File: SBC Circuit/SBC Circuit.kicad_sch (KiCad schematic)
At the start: 21 parts, among them J2 Conn_01x06_Pin, SW1 RESET, U1 MC68000FN, U11 MC34064P, X1 SG-531

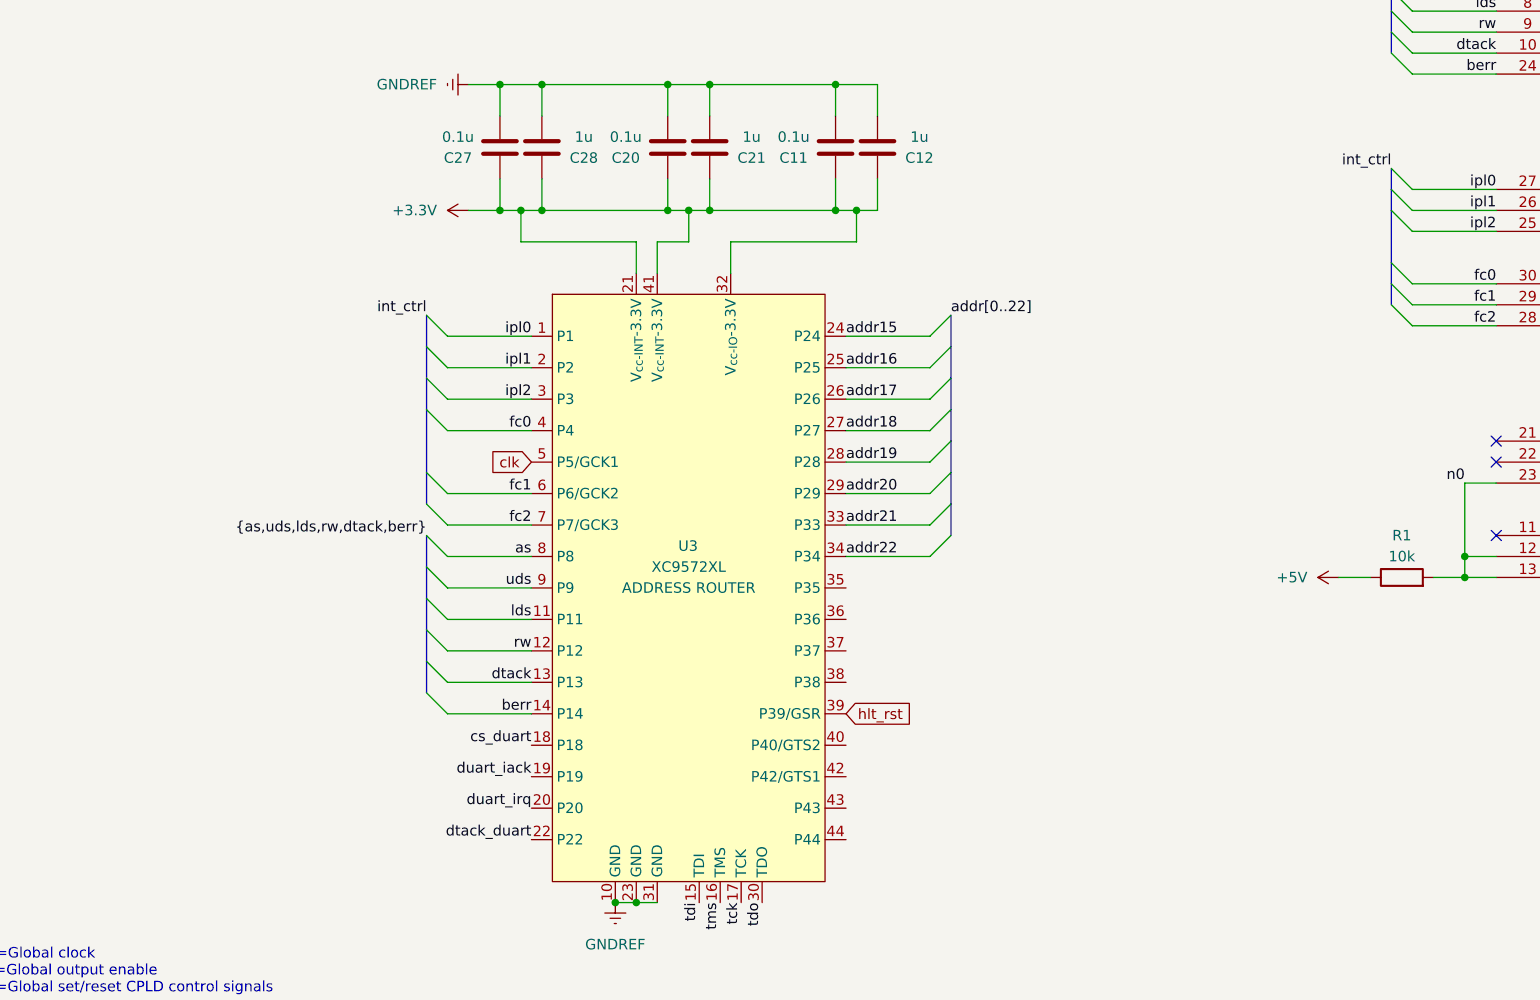
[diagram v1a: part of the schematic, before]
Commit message: New part selections, serial port selection
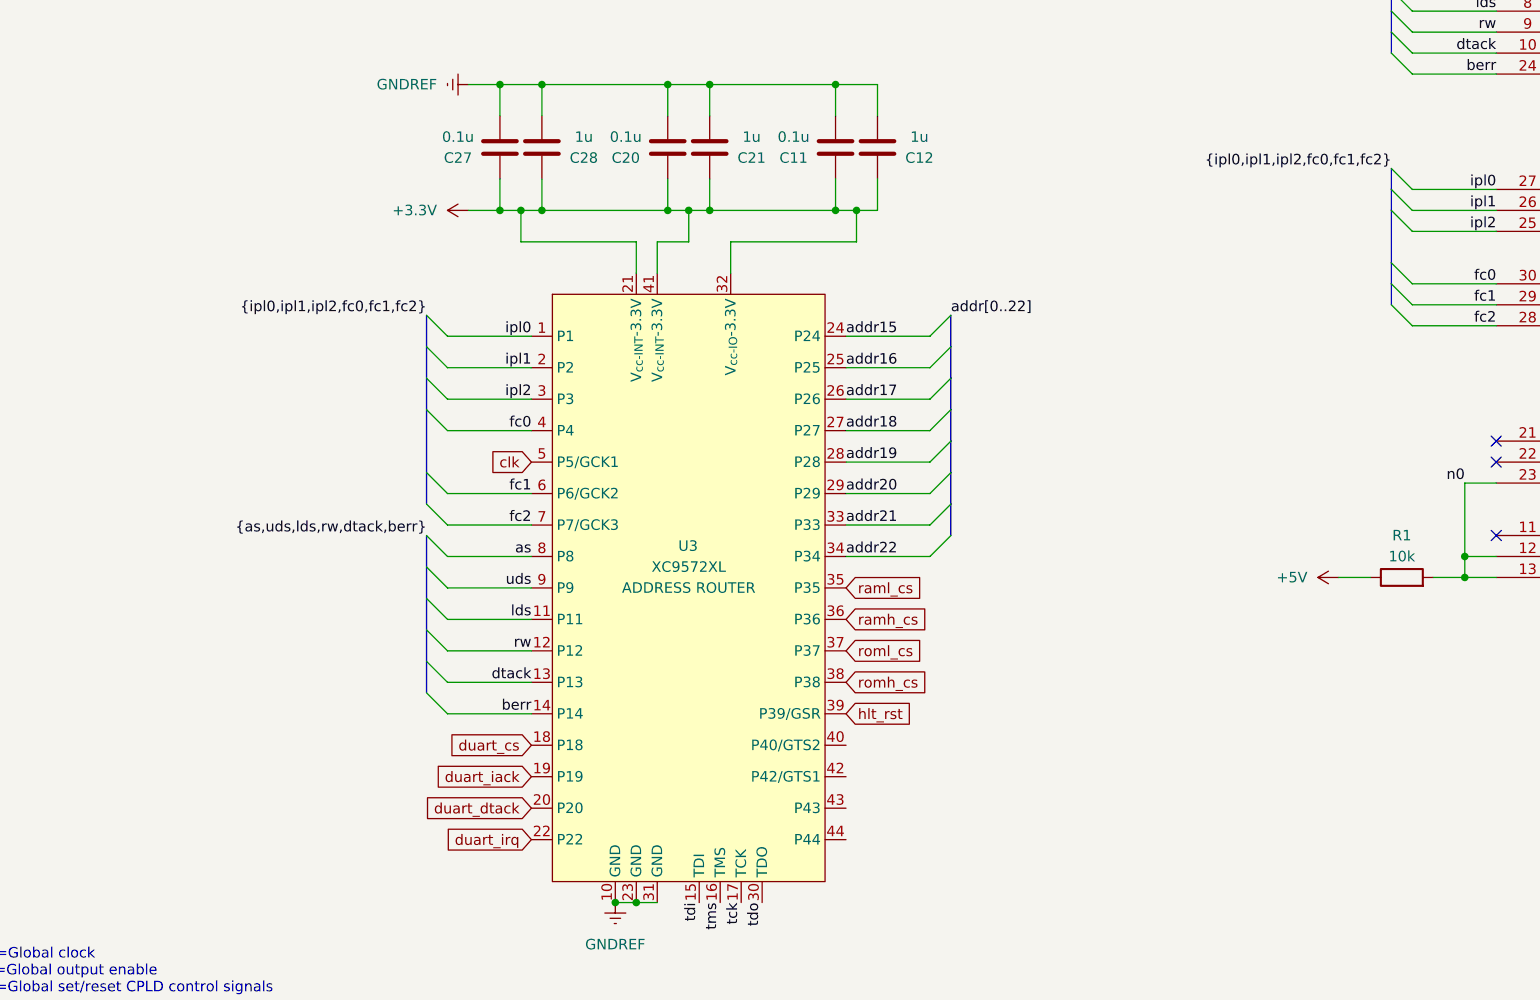
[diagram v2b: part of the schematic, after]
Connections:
- net dtack_duart is gone; now on net duart_irq: U3.22 (P22)
- net duart_irq: no longer U3.20 (P20)
- net raml_cs: now reaches U3.35 (P35)
- net ramh_cs: now reaches U3.36 (P36)
- net roml_cs: now reaches U3.37 (P37)
- net romh_cs: now reaches U3.38 (P38)
- net cs_duart renamed duart_cs
- new net duart_dtack: U3.20 (P20)

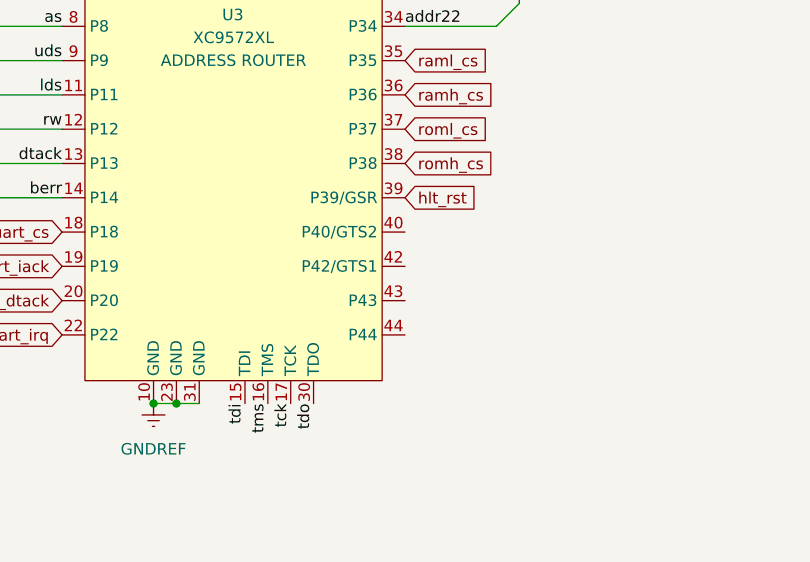
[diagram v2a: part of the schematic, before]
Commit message: Add peripheral headers to schematic
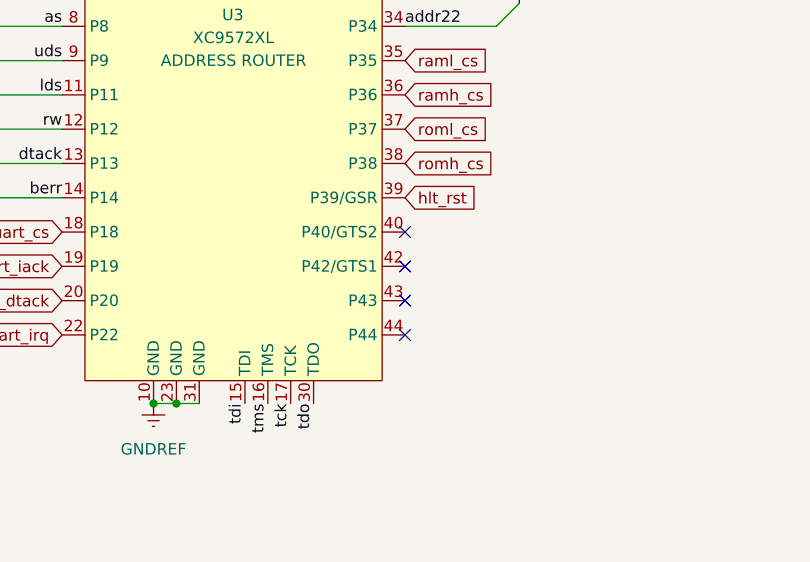
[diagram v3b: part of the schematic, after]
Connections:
- no-connect marks 3 -> 7
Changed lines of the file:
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@@
   (no_connect (at 200.66 127))
   (no_connect (at 200.66 124.46))
+  (no_connect (at 121.92 172.72))
   (no_connect (at 200.66 135.89))
+  (no_connect (at 121.92 168.91))
+  (no_connect (at 121.92 165.1))
+  (no_connect (at 121.92 161.29))
   (bus_entry (at 264.16 55.88) (size -2.54 2.54)
     (stroke (width 0) (type default))

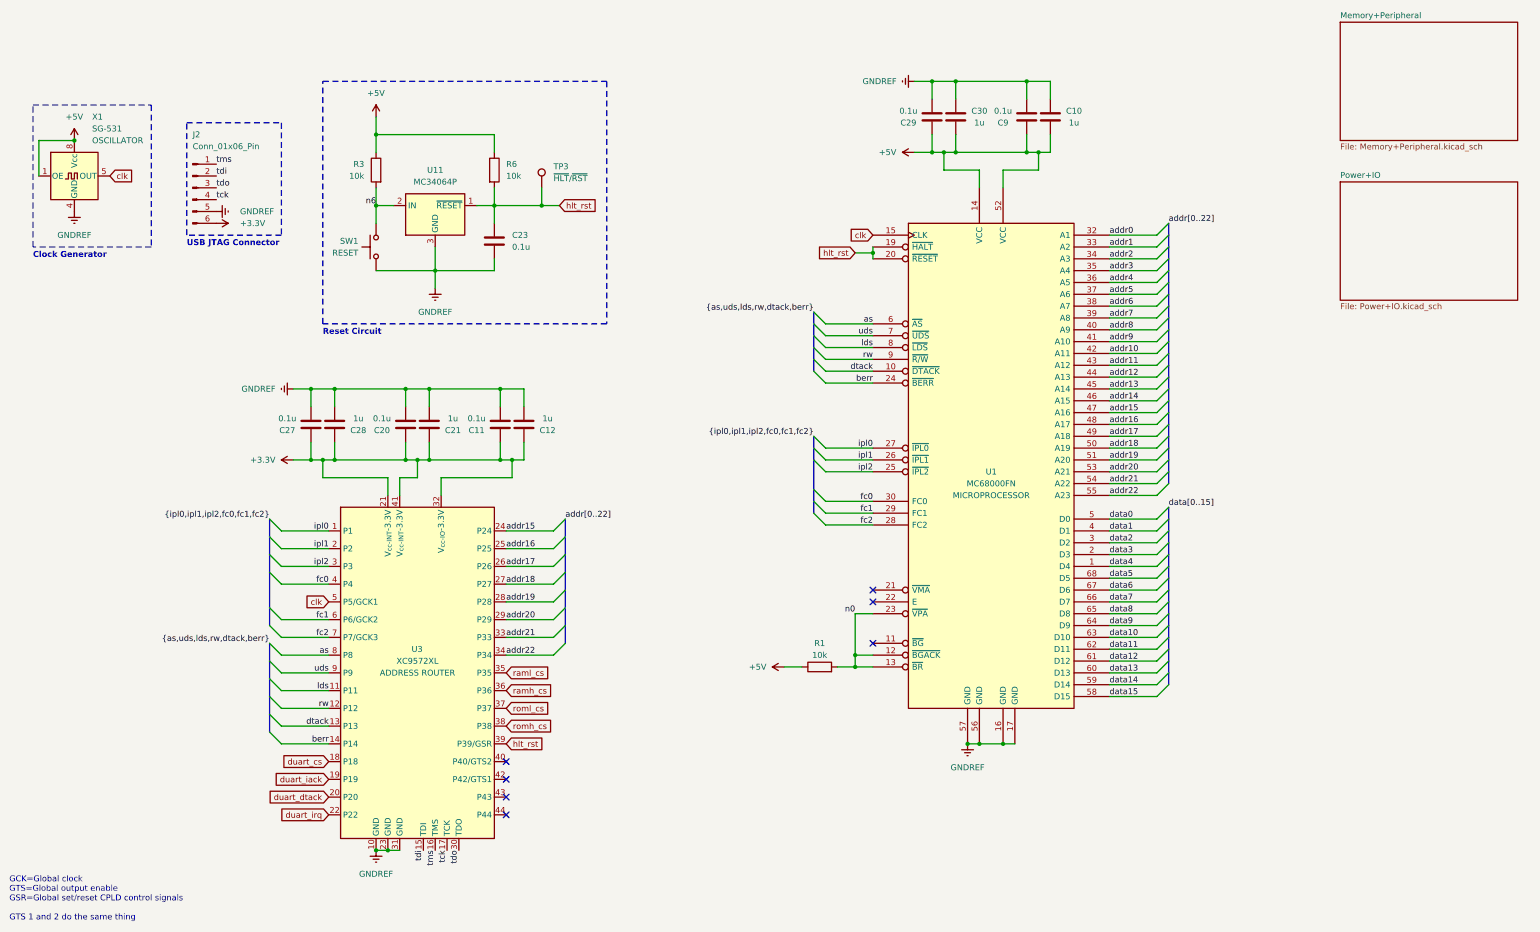
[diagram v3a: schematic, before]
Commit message: Reannotate schematic
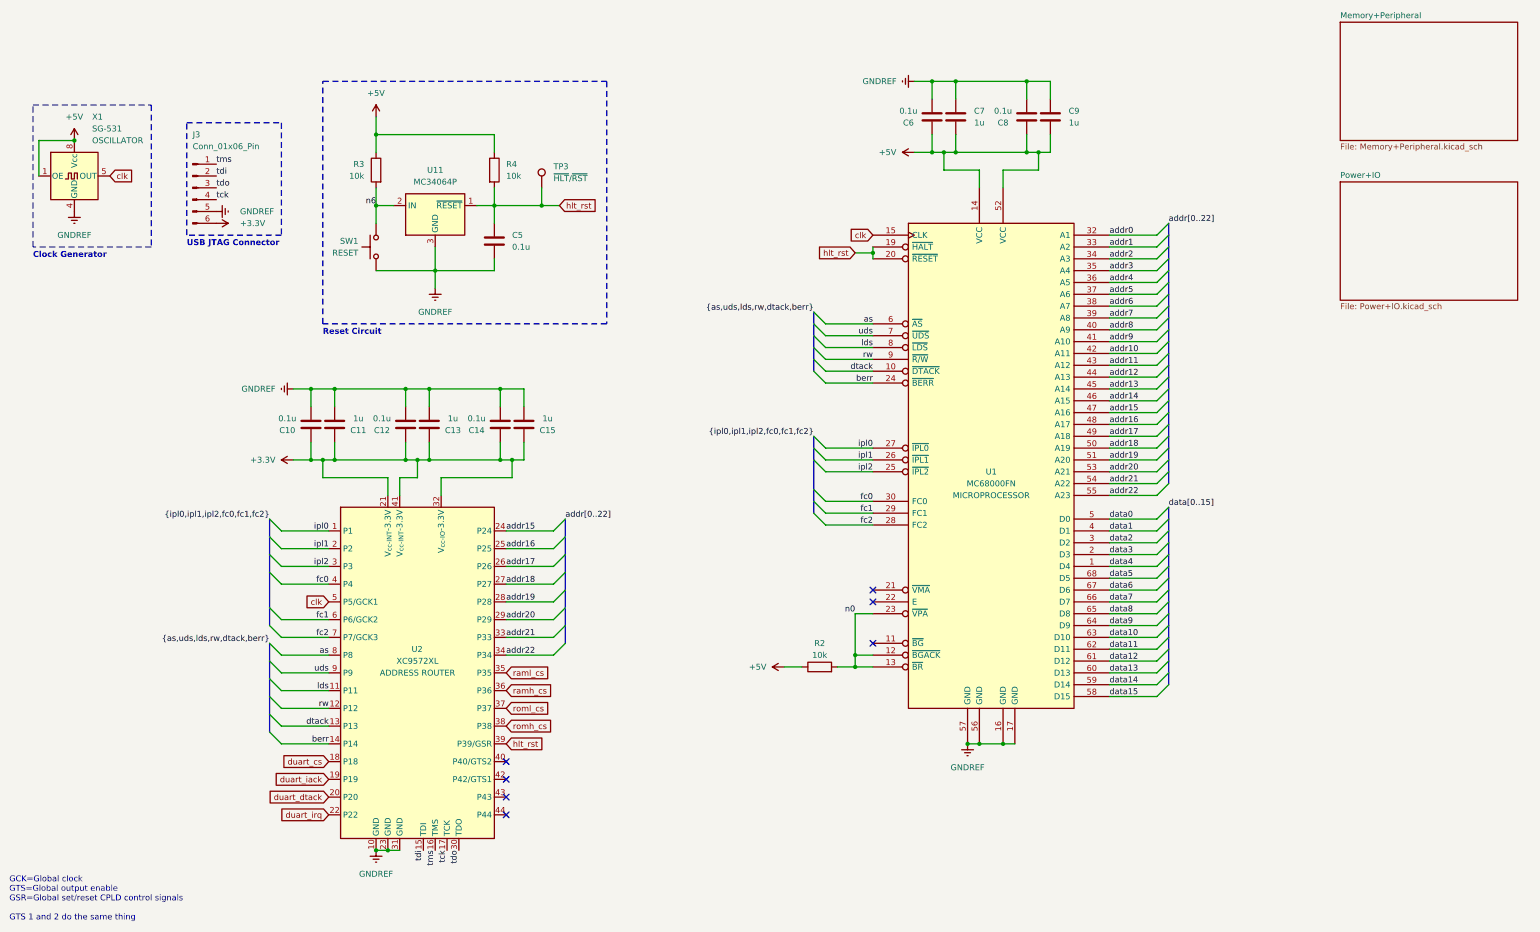
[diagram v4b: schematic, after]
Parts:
- renumbered C27 to C10, C28 to C11, C20 to C12, C21 to C13, C11 to C14, C12 to C15, C23 to C5, C29 to C6, C30 to C7, C9 to C8, C10 to C9, J2 to J3, R1 to R2, R6 to R4, U3 to U2
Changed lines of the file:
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@@
   (symbol (lib_id "CPLD_Xilinx:XC9572XL-PC44") (at 102.87 139.7 0) (unit 1)
     (in_bom yes) (on_board yes) (dnp no)
-    (property "Reference" "U3" (at 101.6 137.16 0)
+    (property "Reference" "U2" (at 101.6 137.16 0)
       (effects (font (size 1.27 1.27)) (justify left))
     )
@@
       (project "SBC Circuit"
         (path "/3db026c4-f98d-4c94-ab2a-d9924b8daebe"
-          (reference "U3") (unit 1)
+          (reference "U2") (unit 1)
         )
       )
@@
   (symbol (lib_id "Device:R") (at 119.38 34.29 0) (unit 1)
     (in_bom yes) (on_board yes) (dnp no)
-    (property "Reference" "R6" (at 121.92 33.02 0)
+    (property "Reference" "R4" (at 121.92 33.02 0)
       (effects (font (size 1.27 1.27)) (justify left))
     )
@@
       (project "SBC Circuit"
         (path "/3db026c4-f98d-4c94-ab2a-d9924b8daebe"
-          (reference "R6") (unit 1)
+          (reference "R4") (unit 1)
         )
       )
@@
   (symbol (lib_id "Device:C") (at 80.01 88.9 180) (unit 1)
     (in_bom yes) (on_board yes) (dnp no)
-    (property "Reference" "C27" (at 74.93 90.17 0)
+    (property "Reference" "C10" (at 74.93 90.17 0)
       (effects (font (size 1.27 1.27)))
     )
@@
       (project "SBC Circuit"
         (path "/3db026c4-f98d-4c94-ab2a-d9924b8daebe"
-          (reference "C27") (unit 1)
+          (reference "C10") (unit 1)
         )
       )
@@
   (symbol (lib_id "Device:C") (at 238.76 22.86 0) (mirror x) (unit 1)
     (in_bom yes) (on_board yes) (dnp no)
-    (property "Reference" "C10" (at 243.84 21.59 0)
+    (property "Reference" "C9" (at 243.84 21.59 0)
       (effects (font (size 1.27 1.27)))
     )
@@
       (project "SBC Circuit"
         (path "/3db026c4-f98d-4c94-ab2a-d9924b8daebe"
-          (reference "C10") (unit 1)
+          (reference "C9") (unit 1)
         )
       )
@@
   (symbol (lib_id "Device:C") (at 120.65 88.9 180) (unit 1)
     (in_bom yes) (on_board yes) (dnp no)
-    (property "Reference" "C11" (at 115.57 90.17 0)
+    (property "Reference" "C14" (at 115.57 90.17 0)
       (effects (font (size 1.27 1.27)))
     )
@@
       (project "SBC Circuit"
         (path "/3db026c4-f98d-4c94-ab2a-d9924b8daebe"
-          (reference "C11") (unit 1)
+          (reference "C14") (unit 1)
         )
       )
@@
   (symbol (lib_id "Device:C") (at 213.36 22.86 180) (unit 1)
     (in_bom yes) (on_board yes) (dnp no)
-    (property "Reference" "C29" (at 208.28 24.13 0)
+    (property "Reference" "C6" (at 208.28 24.13 0)
       (effects (font (size 1.27 1.27)))
     )
@@
       (project "SBC Circuit"
         (path "/3db026c4-f98d-4c94-ab2a-d9924b8daebe"
-          (reference "C29") (unit 1)
+          (reference "C6") (unit 1)
         )
       )
@@
   (symbol (lib_id "Device:C") (at 119.38 49.53 0) (unit 1)
     (in_bom yes) (on_board yes) (dnp no) (fields_autoplaced)
-    (property "Reference" "C23" (at 123.19 48.26 0)
+    (property "Reference" "C5" (at 123.19 48.26 0)
       (effects (font (size 1.27 1.27)) (justify left))
     )
@@
       (project "SBC Circuit"
         (path "/3db026c4-f98d-4c94-ab2a-d9924b8daebe"
-          (reference "C23") (unit 1)
+          (reference "C5") (unit 1)
         )
       )
@@
   (symbol (lib_id "Connector:Conn_01x06_Pin") (at 54.61 38.1 0) (unit 1)
     (in_bom yes) (on_board yes) (dnp no)
-    (property "Reference" "J2" (at 54.61 26.67 0)
+    (property "Reference" "J3" (at 54.61 26.67 0)
       (effects (font (size 1.27 1.27)) (justify left))
     )
@@
       (project "SBC Circuit"
         (path "/3db026c4-f98d-4c94-ab2a-d9924b8daebe"
-          (reference "J2") (unit 1)
+          (reference "J3") (unit 1)
         )
       )
@@
   (symbol (lib_id "Device:C") (at 233.68 22.86 180) (unit 1)
     (in_bom yes) (on_board yes) (dnp no)
-    (property "Reference" "C9" (at 228.6 24.13 0)
+    (property "Reference" "C8" (at 228.6 24.13 0)
       (effects (font (size 1.27 1.27)))
     )
@@
       (project "SBC Circuit"
         (path "/3db026c4-f98d-4c94-ab2a-d9924b8daebe"
-          (reference "C9") (unit 1)
+          (reference "C8") (unit 1)
         )
       )
@@
   (symbol (lib_id "Device:C") (at 105.41 88.9 0) (mirror x) (unit 1)
     (in_bom yes) (on_board yes) (dnp no)
-    (property "Reference" "C21" (at 110.49 90.17 0)
+    (property "Reference" "C13" (at 110.49 90.17 0)
       (effects (font (size 1.27 1.27)))
     )
@@
       (project "SBC Circuit"
         (path "/3db026c4-f98d-4c94-ab2a-d9924b8daebe"
-          (reference "C21") (unit 1)
+          (reference "C13") (unit 1)
         )
       )
@@
   (symbol (lib_id "Device:C") (at 125.73 88.9 0) (mirror x) (unit 1)
     (in_bom yes) (on_board yes) (dnp no)
-    (property "Reference" "C12" (at 130.81 90.17 0)
+    (property "Reference" "C15" (at 130.81 90.17 0)
       (effects (font (size 1.27 1.27)))
     )
@@
       (project "SBC Circuit"
         (path "/3db026c4-f98d-4c94-ab2a-d9924b8daebe"
-          (reference "C12") (unit 1)
+          (reference "C15") (unit 1)
         )
       )
@@
   (symbol (lib_id "Device:R") (at 189.23 140.97 90) (unit 1)
     (in_bom yes) (on_board yes) (dnp no)
-    (property "Reference" "R1" (at 189.23 135.89 90)
+    (property "Reference" "R2" (at 189.23 135.89 90)
       (effects (font (size 1.27 1.27)))
     )
@@
       (project "SBC Circuit"
         (path "/3db026c4-f98d-4c94-ab2a-d9924b8daebe"
-          (reference "R1") (unit 1)
+          (reference "R2") (unit 1)
         )
       )
@@
   (symbol (lib_id "Device:C") (at 100.33 88.9 180) (unit 1)
     (in_bom yes) (on_board yes) (dnp no)
-    (property "Reference" "C20" (at 95.25 90.17 0)
+    (property "Reference" "C12" (at 95.25 90.17 0)
       (effects (font (size 1.27 1.27)))
     )
@@
       (project "SBC Circuit"
         (path "/3db026c4-f98d-4c94-ab2a-d9924b8daebe"
-          (reference "C20") (unit 1)
+          (reference "C12") (unit 1)
         )
       )
@@
   (symbol (lib_id "Device:C") (at 218.44 22.86 0) (mirror x) (unit 1)
     (in_bom yes) (on_board yes) (dnp no)
-    (property "Reference" "C30" (at 223.52 21.59 0)
+    (property "Reference" "C7" (at 223.52 21.59 0)
       (effects (font (size 1.27 1.27)))
     )
@@
       (project "SBC Circuit"
         (path "/3db026c4-f98d-4c94-ab2a-d9924b8daebe"
-          (reference "C30") (unit 1)
+          (reference "C7") (unit 1)
         )
       )
@@
   (symbol (lib_id "Device:C") (at 85.09 88.9 0) (mirror x) (unit 1)
     (in_bom yes) (on_board yes) (dnp no)
-    (property "Reference" "C28" (at 90.17 90.17 0)
+    (property "Reference" "C11" (at 90.17 90.17 0)
       (effects (font (size 1.27 1.27)))
     )
@@
       (project "SBC Circuit"
         (path "/3db026c4-f98d-4c94-ab2a-d9924b8daebe"
-          (reference "C28") (unit 1)
-        )
-      )
+          (reference "C11") (unit 1)
+        )
+      )
